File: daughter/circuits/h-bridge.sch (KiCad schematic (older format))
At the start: 7 parts, among them Q10 Q_NPN_BEC, Q11 Q_DMHC4035LSD, Q9 Q_NPN_BEC

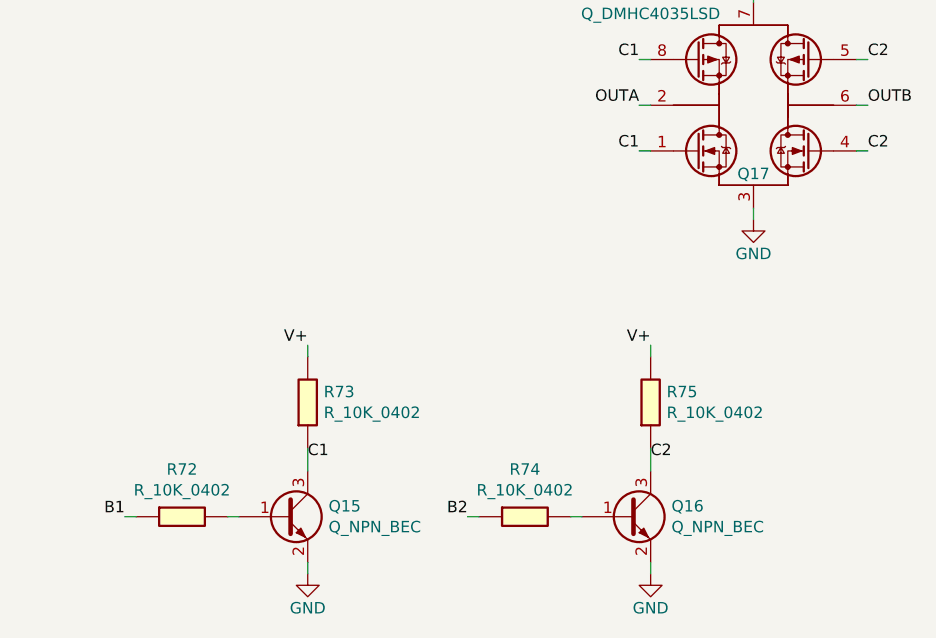
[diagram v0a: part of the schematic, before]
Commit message: finished schematic, working on layout
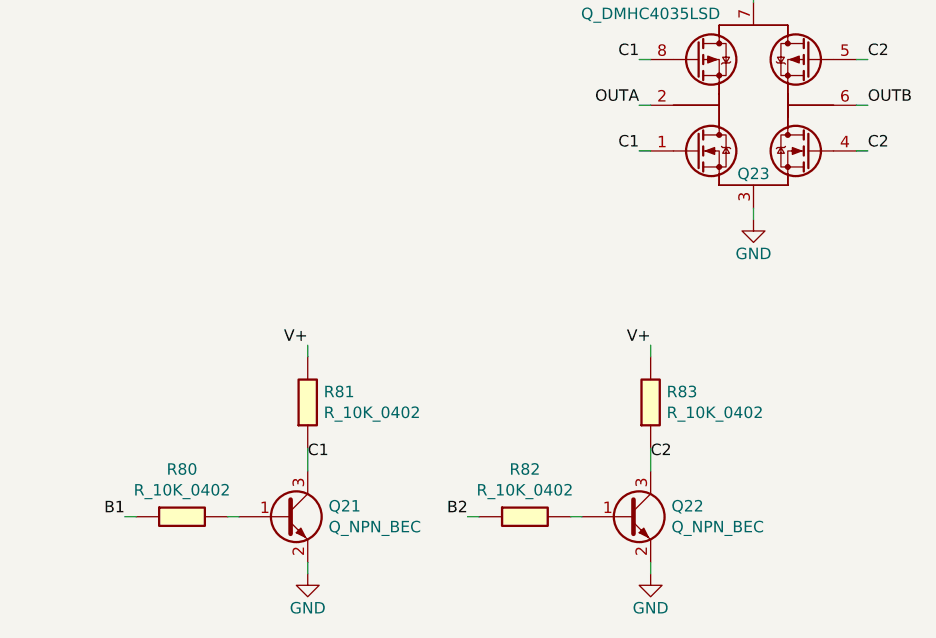
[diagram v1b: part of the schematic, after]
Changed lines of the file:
@@
 $Descr A4 11693 8268
 encoding utf-8
-Sheet 11 14
+Sheet 10 14
 Title ""
 Date ""
@@
 AR Path="/601F213A/60537FF7/605507A9" Ref="Q20"  Part="1"
 AR Path="/601F213A/607B7BA9/605507A9" Ref="Q23"  Part="1"
-F 0 "Q17" H 5550 2450 50  0000 C CNN
+F 0 "Q23" H 5550 2450 50  0000 C CNN
 F 1 "Q_DMHC4035LSD" H 5100 3150 50  0000 C CNN
 F 2 "Package_SO:SOP-8_3.9x4.9mm_P1.27mm" H 4700 3550 50  0001 L CIN
@@
 AR Path="/601F213A/60537FF7/6055EDDA" Ref="Q19"  Part="1"
 AR Path="/601F213A/607B7BA9/6055EDDA" Ref="Q22"  Part="1"
-F 0 "Q16" H 5191 3996 50  0000 L CNN
+F 0 "Q22" H 5191 3996 50  0000 L CNN
 F 1 "Q_NPN_BEC" H 5191 3905 50  0000 L CNN
 F 2 "Package_TO_SOT_SMD:SOT-23" H 5200 4050 50  0001 C CNN
@@
 AR Path="/601F213A/60537FF7/605659CE" Ref="R79"  Part="1"
 AR Path="/601F213A/607B7BA9/605659CE" Ref="R83"  Part="1"
-F 0 "R75" H 5170 3496 50  0000 L CNN
+F 0 "R83" H 5170 3496 50  0000 L CNN
 F 1 "R_10K_0402" H 5170 3405 50  0000 L CNN
 F 2 "Resistor_SMD:R_0402_1005Metric_Pad0.72x0.64mm_HandSolder" V 5030 3450 50  0001 C CNN
@@
 AR Path="/601F213A/60537FF7/6056BCEC" Ref="R78"  Part="1"
 AR Path="/601F213A/607B7BA9/6056BCEC" Ref="R82"  Part="1"
-F 0 "R74" V 4343 3950 50  0000 C CNN
+F 0 "R82" V 4343 3950 50  0000 C CNN
 F 1 "R_10K_0402" V 4434 3950 50  0000 C CNN
 F 2 "Resistor_SMD:R_0402_1005Metric_Pad0.72x0.64mm_HandSolder" V 4480 3950 50  0001 C CNN
@@
 AR Path="/601F213A/60537FF7/605EA495" Ref="#PWR0115"  Part="1"
 AR Path="/601F213A/607B7BA9/605EA495" Ref="#PWR0118"  Part="1"
-F 0 "#PWR0112" H 5100 3950 50  0001 C CNN
+F 0 "#PWR0118" H 5100 3950 50  0001 C CNN
 F 1 "GND" H 5100 4050 50  0000 C CNN
 F 2 "" H 5100 4200 50  0000 C CNN
@@
 AR Path="/601F213A/60537FF7/6062E0E9" Ref="Q18"  Part="1"
 AR Path="/601F213A/607B7BA9/6062E0E9" Ref="Q21"  Part="1"
-F 0 "Q15" H 3691 3996 50  0000 L CNN
+F 0 "Q21" H 3691 3996 50  0000 L CNN
 F 1 "Q_NPN_BEC" H 3691 3905 50  0000 L CNN
 F 2 "Package_TO_SOT_SMD:SOT-23" H 3700 4050 50  0001 C CNN
@@
 AR Path="/601F213A/60537FF7/6062E29F" Ref="R77"  Part="1"
 AR Path="/601F213A/607B7BA9/6062E29F" Ref="R81"  Part="1"
-F 0 "R73" H 3670 3496 50  0000 L CNN
+F 0 "R81" H 3670 3496 50  0000 L CNN
 F 1 "R_10K_0402" H 3670 3405 50  0000 L CNN
 F 2 "Resistor_SMD:R_0402_1005Metric_Pad0.72x0.64mm_HandSolder" V 3530 3450 50  0001 C CNN
@@
 AR Path="/601F213A/60537FF7/6062E2AB" Ref="R76"  Part="1"
 AR Path="/601F213A/607B7BA9/6062E2AB" Ref="R80"  Part="1"
-F 0 "R72" V 2843 3950 50  0000 C CNN
+F 0 "R80" V 2843 3950 50  0000 C CNN
 F 1 "R_10K_0402" V 2934 3950 50  0000 C CNN
 F 2 "Resistor_SMD:R_0402_1005Metric_Pad0.72x0.64mm_HandSolder" V 2980 3950 50  0001 C CNN
@@
 AR Path="/601F213A/60537FF7/6062E2B6" Ref="#PWR0114"  Part="1"
 AR Path="/601F213A/607B7BA9/6062E2B6" Ref="#PWR0117"  Part="1"
-F 0 "#PWR0111" H 3600 3950 50  0001 C CNN
+F 0 "#PWR0117" H 3600 3950 50  0001 C CNN
 F 1 "GND" H 3600 4050 50  0000 C CNN
 F 2 "" H 3600 4200 50  0000 C CNN
@@
 AR Path="/601F213A/60537FF7/6066D64E" Ref="#PWR0116"  Part="1"
 AR Path="/601F213A/607B7BA9/6066D64E" Ref="#PWR0119"  Part="1"
-F 0 "#PWR0113" H 5550 2400 50  0001 C CNN
+F 0 "#PWR0119" H 5550 2400 50  0001 C CNN
 F 1 "GND" H 5550 2500 50  0000 C CNN
 F 2 "" H 5550 2650 50  0000 C CNN

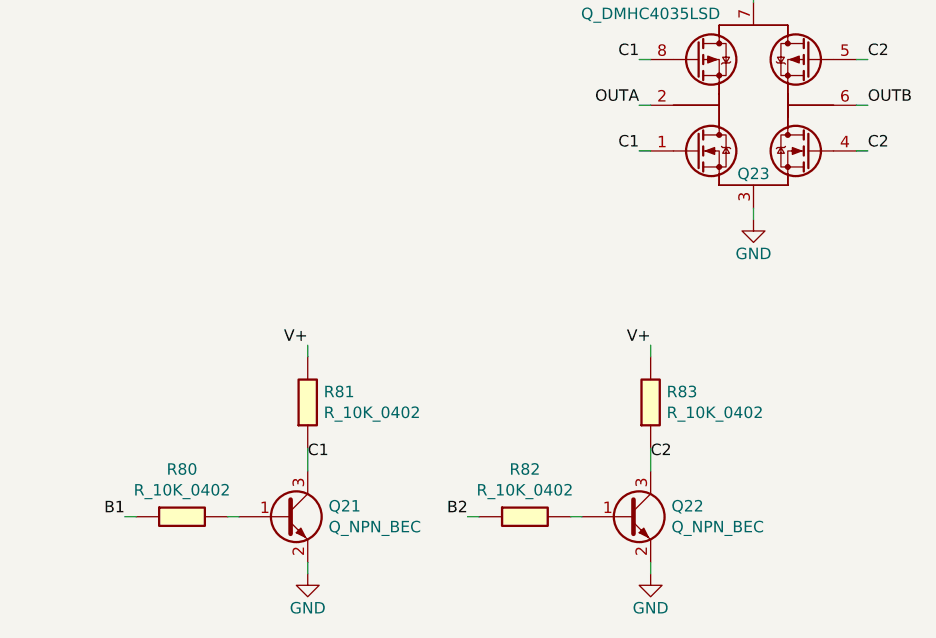
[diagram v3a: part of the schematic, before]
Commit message: Added external amp trigger code and circuit to PCB. Made some layout modifications.
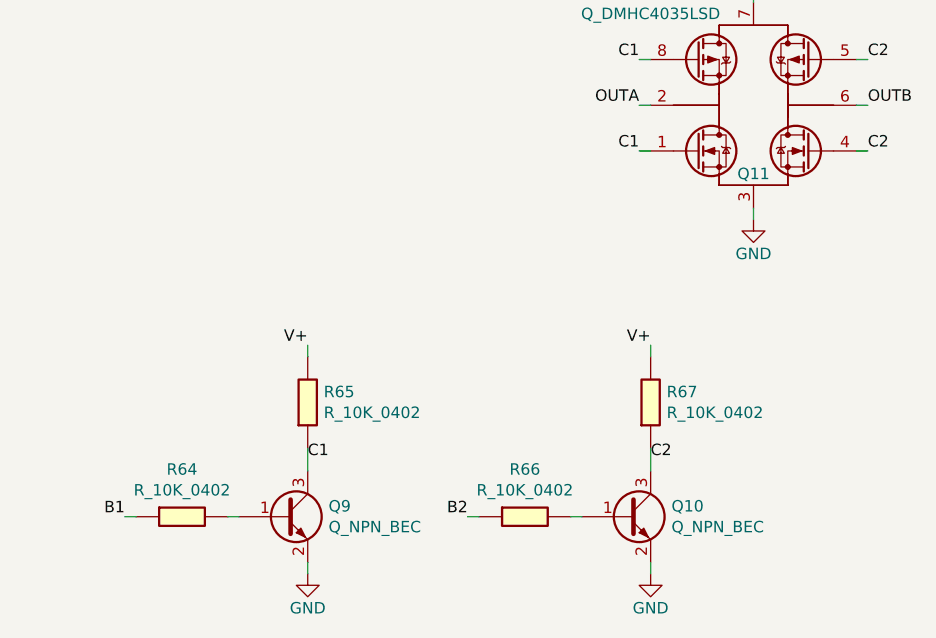
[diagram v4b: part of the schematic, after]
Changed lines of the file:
@@
 AR Path="/601F213A/60537FF7/605507A9" Ref="Q20"  Part="1"
 AR Path="/601F213A/607B7BA9/605507A9" Ref="Q23"  Part="1"
-F 0 "Q23" H 5550 2450 50  0000 C CNN
+F 0 "Q11" H 5550 2450 50  0000 C CNN
 F 1 "Q_DMHC4035LSD" H 5100 3150 50  0000 C CNN
 F 2 "Package_SO:SOP-8_3.9x4.9mm_P1.27mm" H 4700 3550 50  0001 L CIN
@@
 AR Path="/601F213A/60537FF7/6055EDDA" Ref="Q19"  Part="1"
 AR Path="/601F213A/607B7BA9/6055EDDA" Ref="Q22"  Part="1"
-F 0 "Q22" H 5191 3996 50  0000 L CNN
+F 0 "Q10" H 5191 3996 50  0000 L CNN
 F 1 "Q_NPN_BEC" H 5191 3905 50  0000 L CNN
 F 2 "Package_TO_SOT_SMD:SOT-23" H 5200 4050 50  0001 C CNN
@@
 AR Path="/601F213A/60537FF7/605659CE" Ref="R79"  Part="1"
 AR Path="/601F213A/607B7BA9/605659CE" Ref="R83"  Part="1"
-F 0 "R83" H 5170 3496 50  0000 L CNN
+F 0 "R67" H 5170 3496 50  0000 L CNN
 F 1 "R_10K_0402" H 5170 3405 50  0000 L CNN
 F 2 "Resistor_SMD:R_0402_1005Metric_Pad0.72x0.64mm_HandSolder" V 5030 3450 50  0001 C CNN
@@
 AR Path="/601F213A/60537FF7/6056BCEC" Ref="R78"  Part="1"
 AR Path="/601F213A/607B7BA9/6056BCEC" Ref="R82"  Part="1"
-F 0 "R82" V 4343 3950 50  0000 C CNN
+F 0 "R66" V 4343 3950 50  0000 C CNN
 F 1 "R_10K_0402" V 4434 3950 50  0000 C CNN
 F 2 "Resistor_SMD:R_0402_1005Metric_Pad0.72x0.64mm_HandSolder" V 4480 3950 50  0001 C CNN
@@
 AR Path="/601F213A/60537FF7/6062E0E9" Ref="Q18"  Part="1"
 AR Path="/601F213A/607B7BA9/6062E0E9" Ref="Q21"  Part="1"
-F 0 "Q21" H 3691 3996 50  0000 L CNN
+F 0 "Q9" H 3691 3996 50  0000 L CNN
 F 1 "Q_NPN_BEC" H 3691 3905 50  0000 L CNN
 F 2 "Package_TO_SOT_SMD:SOT-23" H 3700 4050 50  0001 C CNN
@@
 AR Path="/601F213A/60537FF7/6062E29F" Ref="R77"  Part="1"
 AR Path="/601F213A/607B7BA9/6062E29F" Ref="R81"  Part="1"
-F 0 "R81" H 3670 3496 50  0000 L CNN
+F 0 "R65" H 3670 3496 50  0000 L CNN
 F 1 "R_10K_0402" H 3670 3405 50  0000 L CNN
 F 2 "Resistor_SMD:R_0402_1005Metric_Pad0.72x0.64mm_HandSolder" V 3530 3450 50  0001 C CNN
@@
 AR Path="/601F213A/60537FF7/6062E2AB" Ref="R76"  Part="1"
 AR Path="/601F213A/607B7BA9/6062E2AB" Ref="R80"  Part="1"
-F 0 "R80" V 2843 3950 50  0000 C CNN
+F 0 "R64" V 2843 3950 50  0000 C CNN
 F 1 "R_10K_0402" V 2934 3950 50  0000 C CNN
 F 2 "Resistor_SMD:R_0402_1005Metric_Pad0.72x0.64mm_HandSolder" V 2980 3950 50  0001 C CNN

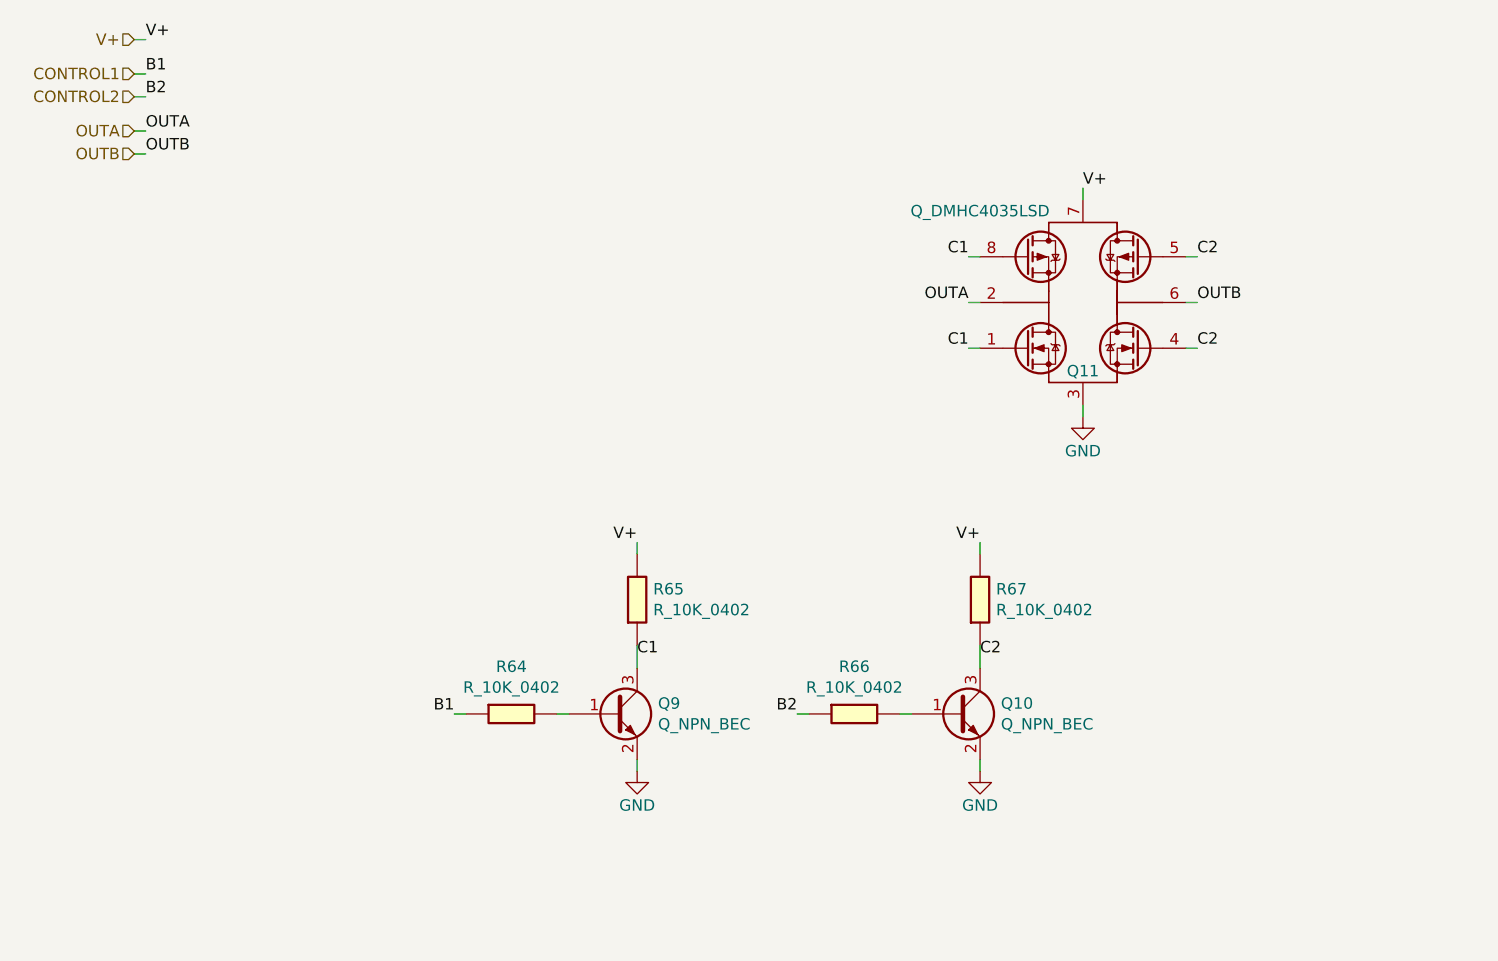
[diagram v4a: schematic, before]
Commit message: Using npn-pnp high side switch for ext amp trigger.
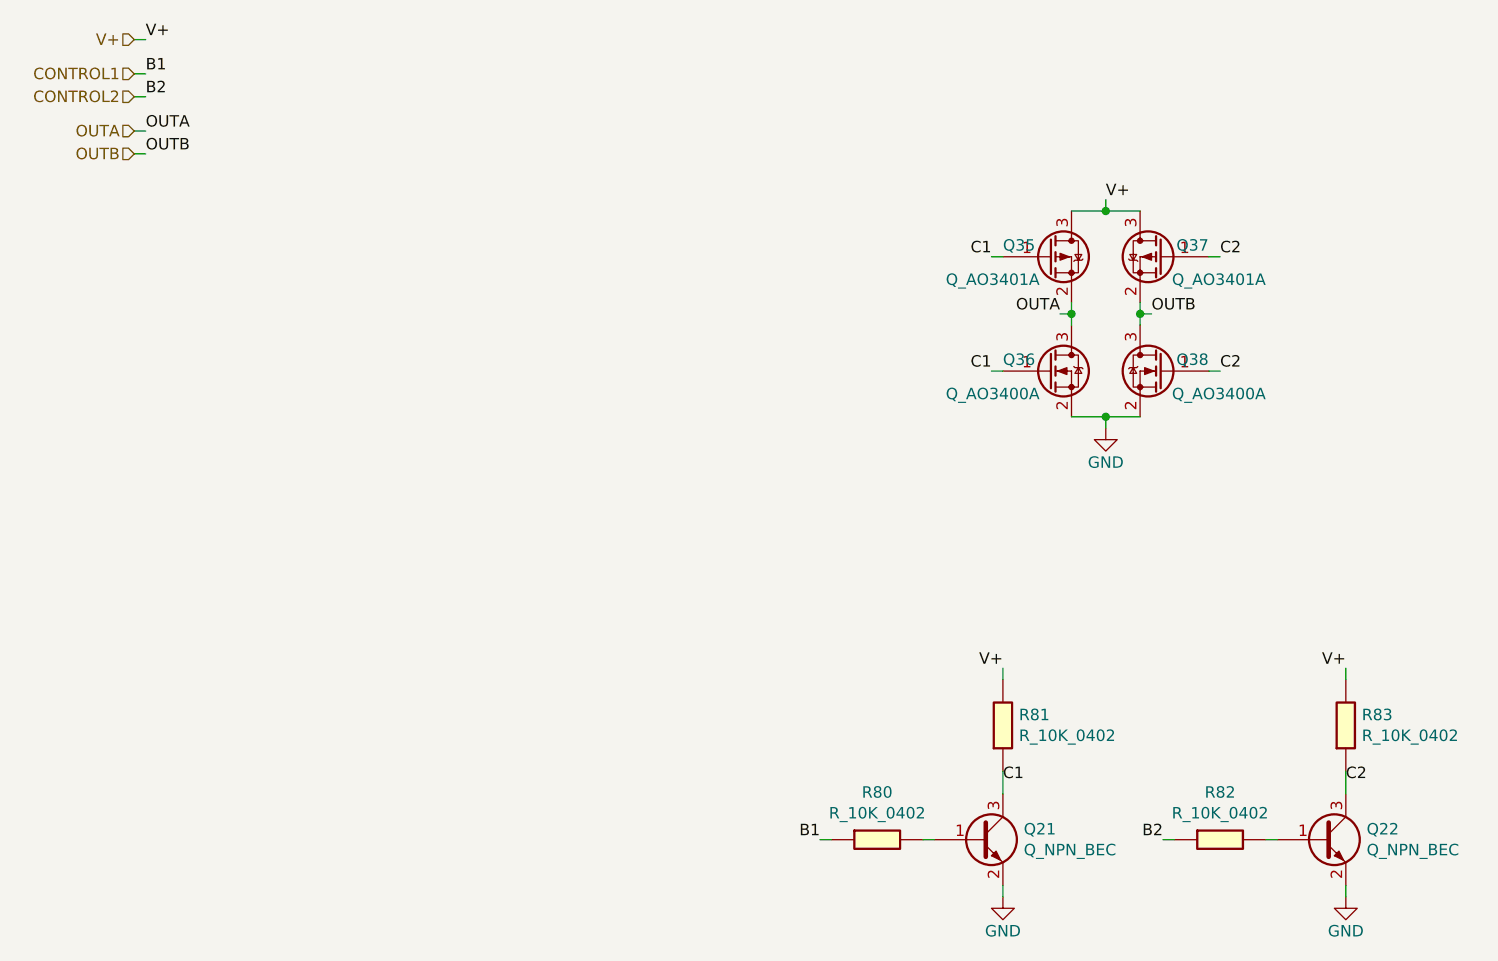
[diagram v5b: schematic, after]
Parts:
- removed Q11: Q_DMHC4035LSD, Package_SO:SOP-8_3.9x4.9mm_P1.27mm, symbol Open_Automation:Q_DMHC4035LSD
- added Q11, Q17: Q_AO3401A, Package_TO_SOT_SMD:SOT-23, symbol Open_Automation:Q_AO3401A
- added Q14, Q20: Q_AO3400A, Package_TO_SOT_SMD:SOT-23, symbol Open_Automation:Q_AO3400A
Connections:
- net C1: now also Q11.1 (G), Q14.1 (G)
- net C2: now also Q17.1 (G), Q20.1 (G)
- net GND: now also Q14.2 (S), Q20.2 (S)
- net OUTA: now also Q11.2 (S), Q14.3 (D)
- net OUTB: now also Q17.2 (S), Q20.3 (D)
- net V+: now also Q11.3 (D), Q17.3 (D)
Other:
- moved on the sheet: Q21, Q22, R80, R81, R82, R83
